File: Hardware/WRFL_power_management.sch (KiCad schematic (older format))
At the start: 43 parts, among them P1 JST_XH_2, P17 1x2_2_54_MALE, P2 TEST_POINT, P3 TEST_POINT, P4 JST_XH_2, P5 TEST_POINT, P6 TEST_POINT, P7 TEST_POINT, Q1 SI1012CR, Q2 SI2333DDS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

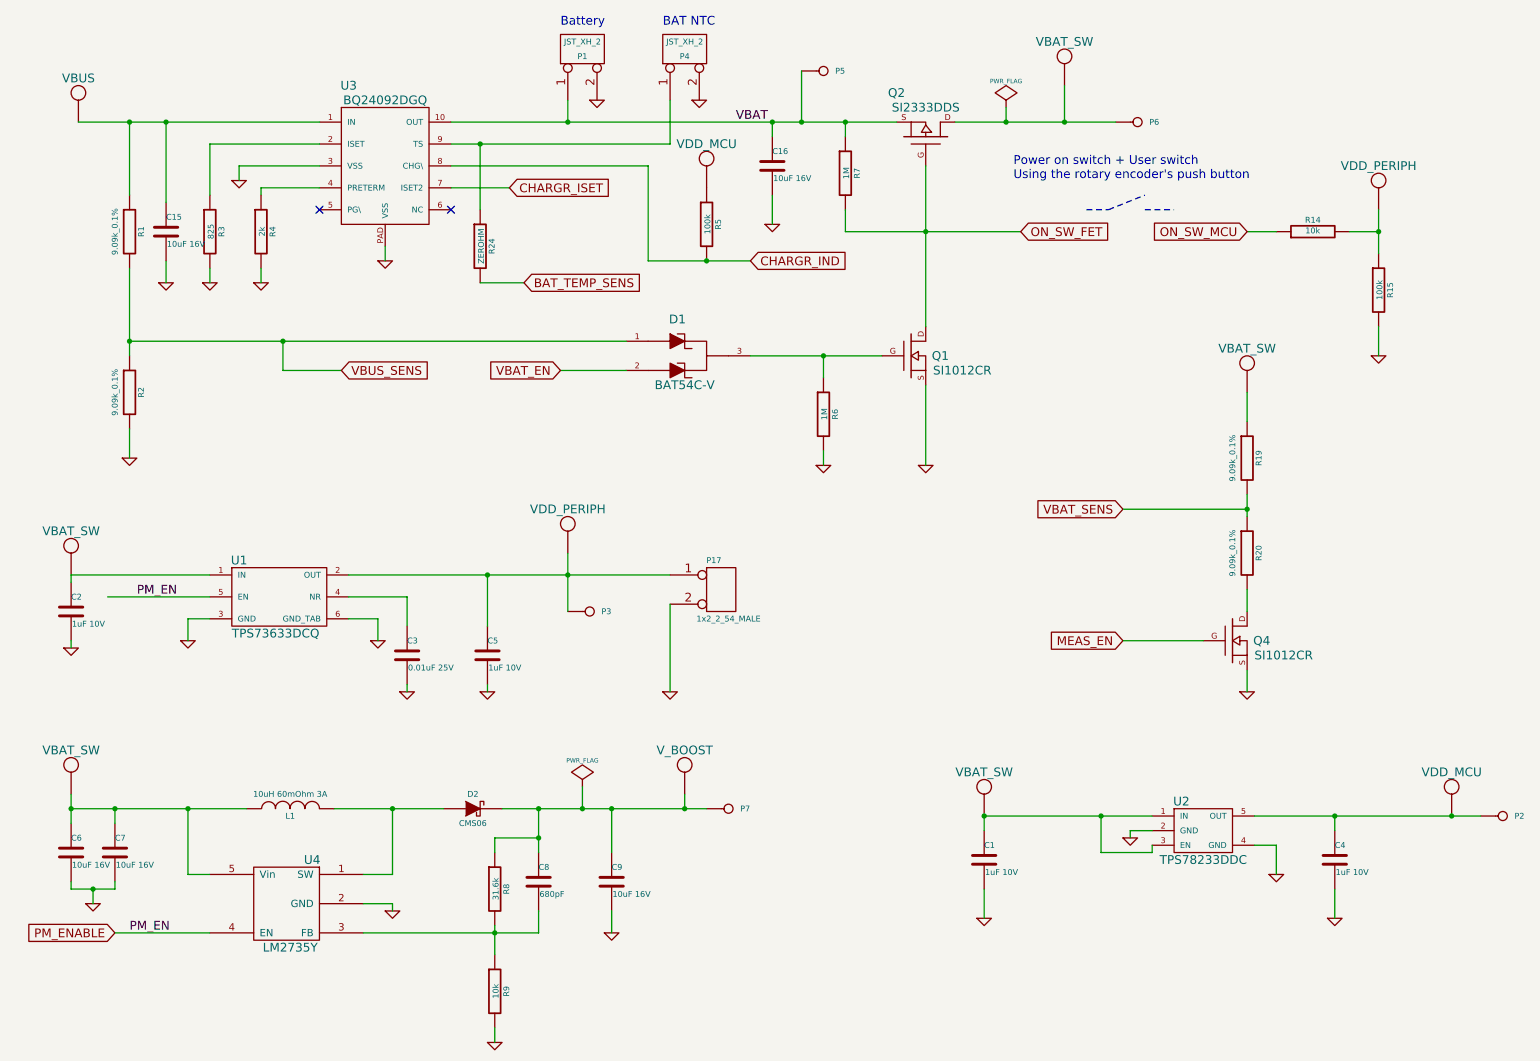
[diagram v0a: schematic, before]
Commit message: 3d Kalman filter progress + minor sch
-moving towards a matrix (CMSIS) based kalman implementation
-cosmetic schematic  changes
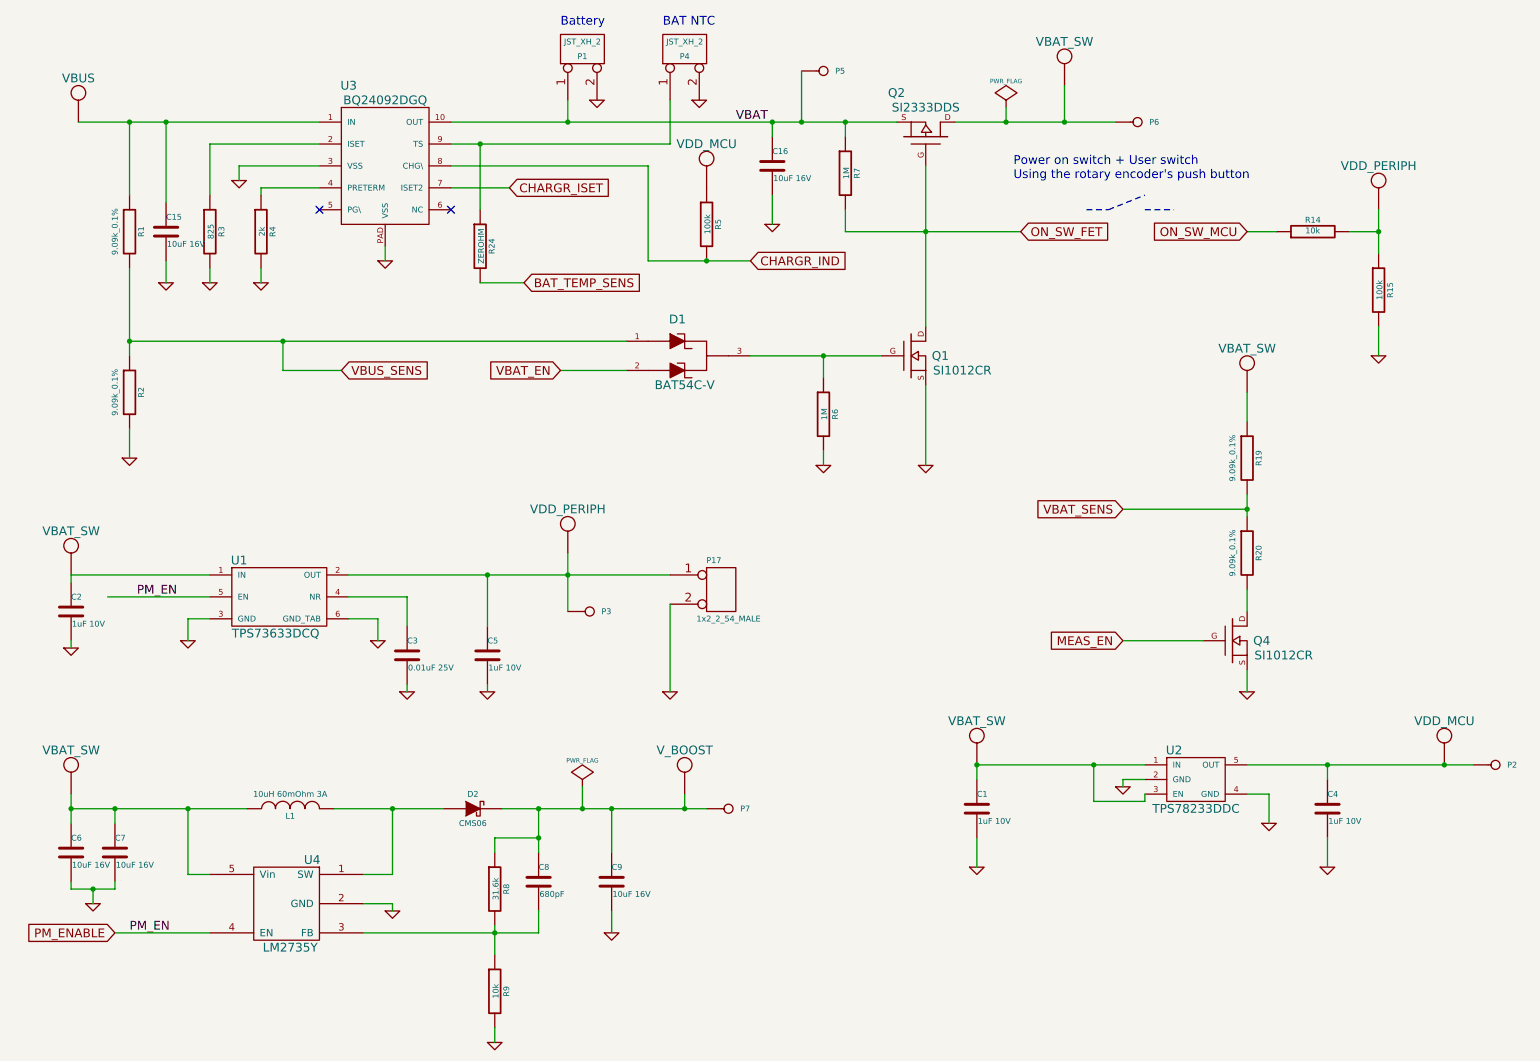
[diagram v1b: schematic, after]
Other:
- moved on the sheet: C1, C4, P2, U2
